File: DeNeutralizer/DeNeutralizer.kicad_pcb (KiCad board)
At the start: 2 copper layers, 27.9 x 72 mm, 20 parts, among them J1 Screw_Terminal_01x03, J2 Screw_Terminal_01x03, J3 Screw_Terminal_01x03, J4 Screw_Terminal_01x03, J5 Screw_Terminal_01x02, J6 Screw_Terminal_01x05, J7 Screw_Terminal_01x02, U1 PC817

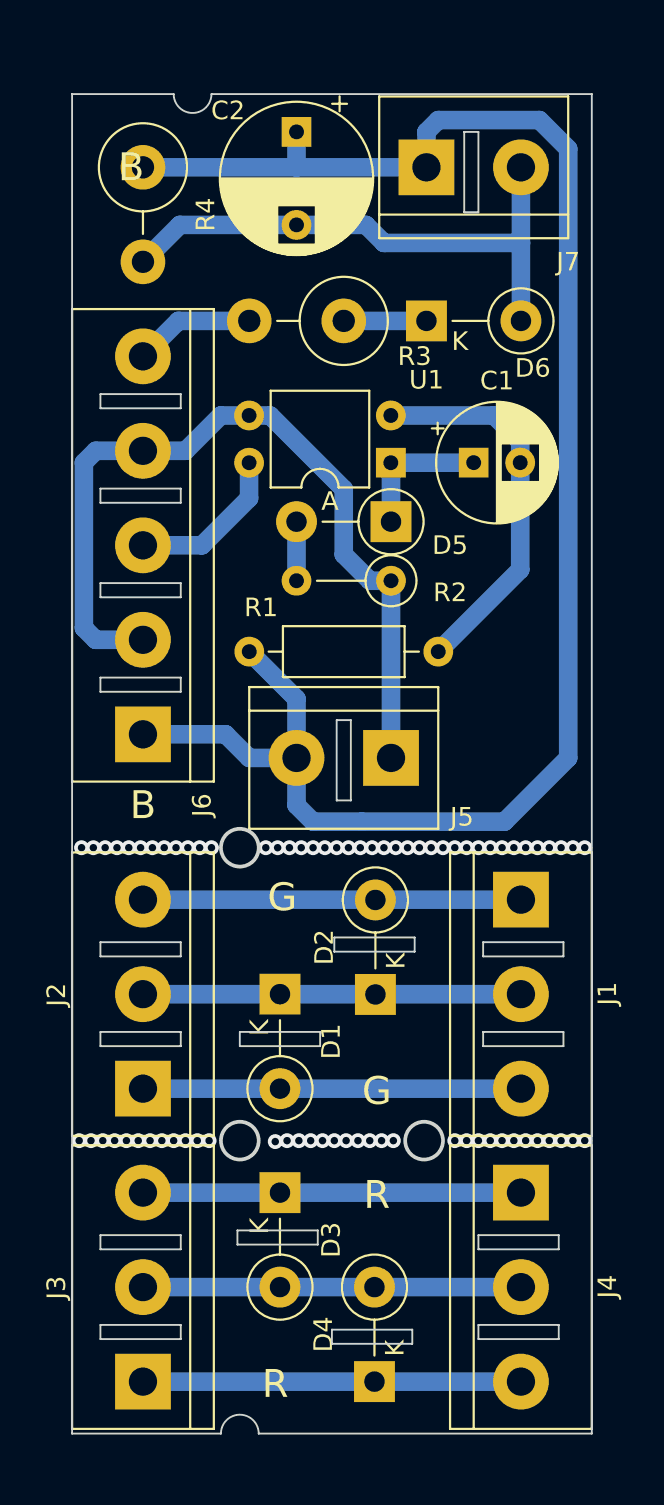
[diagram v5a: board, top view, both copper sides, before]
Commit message: Add spark gaps
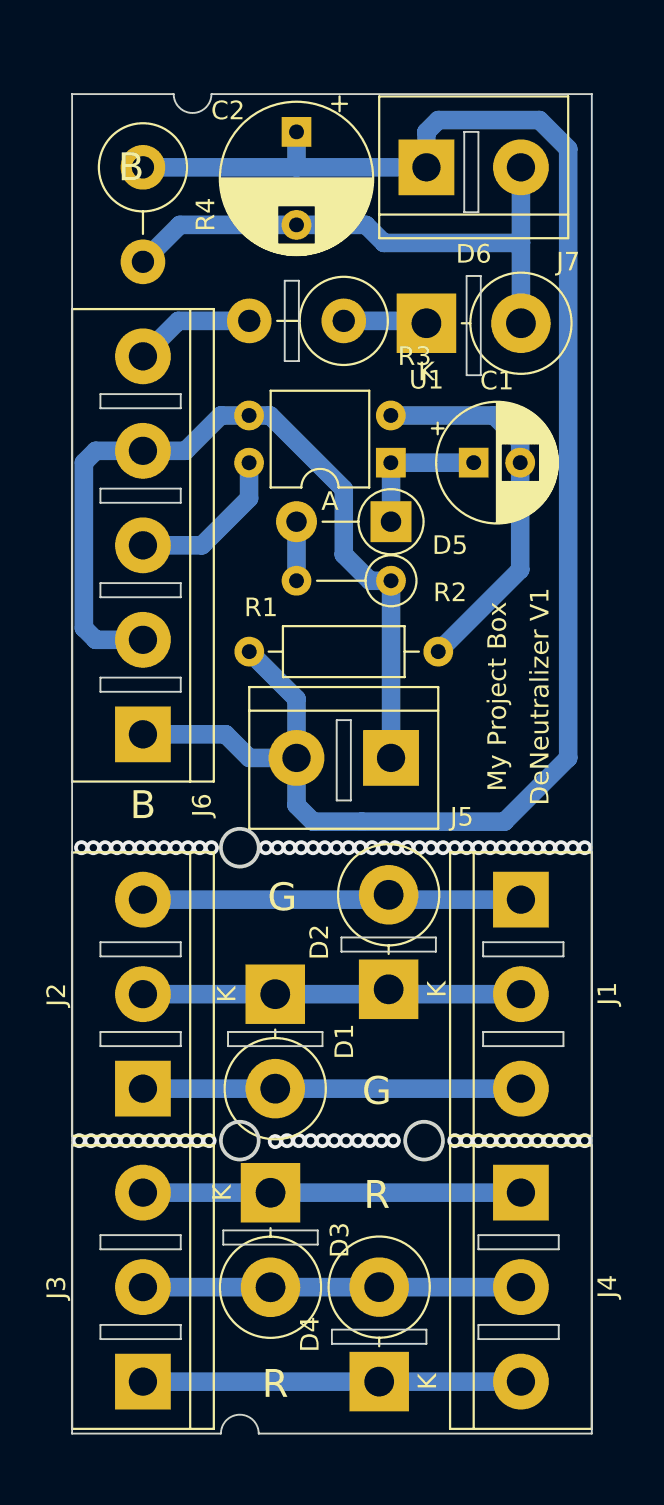
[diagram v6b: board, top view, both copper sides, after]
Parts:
- D1, D2, D3, D4, D6: value 1N4007 -> 1N5408; footprint Diode_THT:D_DO-41_SOD81_P5.08mm_Vertical_KathodeUp -> Diode_THT:D_DO-201AD_P5.08mm_Vertical_KathodeUp
- moved D2 0.76 mm to (133.9, 116.6)
- moved D3 0.51 mm to (127.5, 127.5)
- moved D1 0.25 mm to (127.8, 116.8)
- moved D4 0.25 mm to (133.3, 137.7)
- moved D6 0.13 mm to (135.9, 80.8)
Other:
- outline, holes or cut-outs redrawn
- board text added: "DeNeutralizer V1"
- board text added: "My Project Box"

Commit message: Add jumper and for switcihing between modes and crt for external ripple capacitor
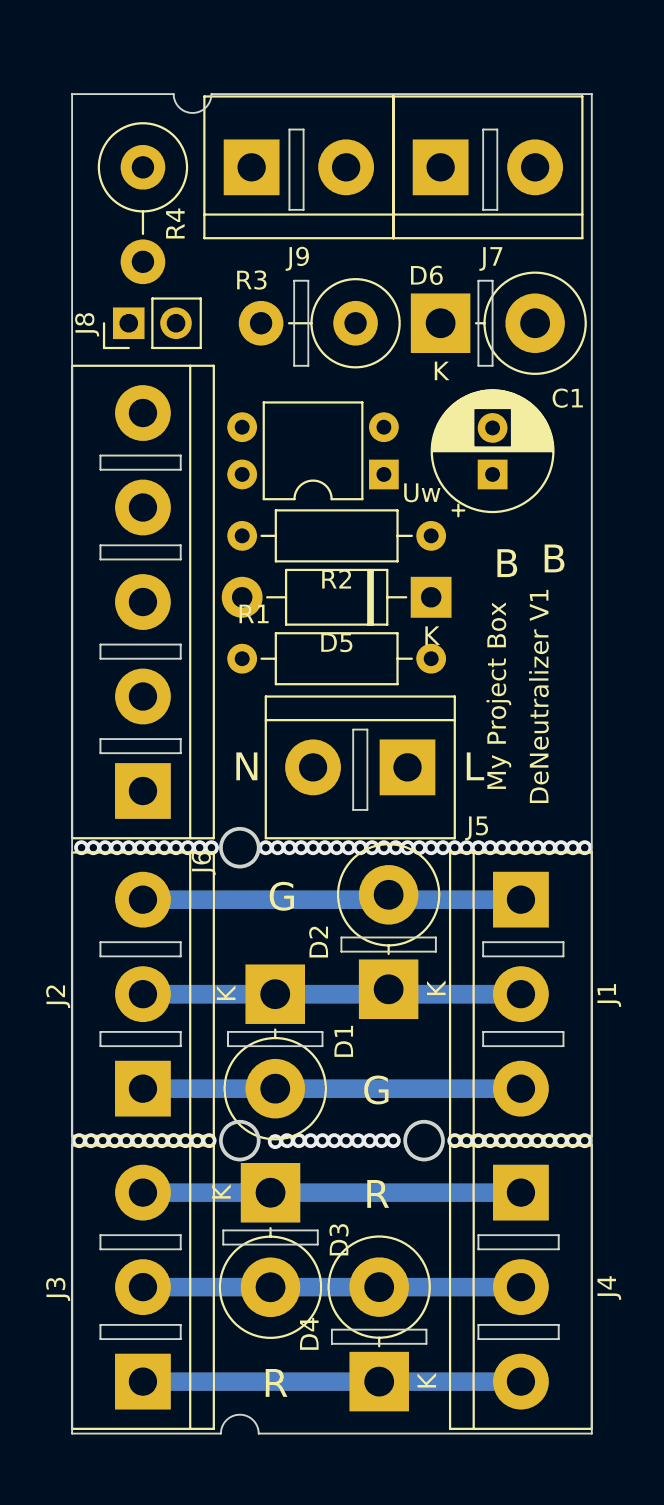
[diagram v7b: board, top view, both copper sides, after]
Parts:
- removed C2: C_Polarized, Capacitor_THT:CP_Radial_D8.0mm_P5.00mm
- added J8: Conn_01x02_Male, Connector_PinHeader_2.54mm:PinHeader_1x02_P2.54mm_Vertical, F.Cu at (119.9, 80.8)
- added J9: Ripple-Cap, TerminalBlock:TerminalBlock_bornier-2_P5.08mm, F.Cu at (126.5, 72.4)
- D5: footprint Diode_THT:D_DO-41_SOD81_P5.08mm_Vertical_AnodeUp -> Diode_THT:D_DO-41_SOD81_P10.16mm_Horizontal
- R2: footprint Resistor_THT:R_Axial_DIN0207_L6.3mm_D2.5mm_P5.08mm_Vertical -> Resistor_THT:R_Axial_DIN0207_L6.3mm_D2.5mm_P10.16mm_Horizontal
- moved D5 4.60 mm to (136.1, 95.5)
- moved R2 3.24 mm to (136.1, 92.2)
- moved J6 3.05 mm to (120.7, 105.9)
- moved C1 1.20 mm to (139.4, 88.9), turned to 90 degrees
- moved J5 1.02 mm to (134.9, 104.6)
- moved D6 0.76 mm to (136.7, 80.8)
- moved J7 0.76 mm to (136.7, 72.4)
- moved Uw 0.73 mm to (133.6, 88.9)
- moved R3 0.65 mm to (132.1, 80.8)
- moved R1 0.54 mm to (126.0, 98.8)
- renumbered U1 to Uw
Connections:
- D5 pad 1: Net-(C1-Pad1) -> Net-(R2-Pad1)
- D5 pad 2: Net-(D5-Pad2) -> Net-(J5-Pad1)
- J6 pad 4: Net-(J5-Pad1) -> Net-(J6-Pad4)
- R2 pad 1: Net-(J5-Pad1) -> Net-(R2-Pad1)
- R2 pad 2: Net-(D5-Pad2) -> Net-(C1-Pad1)
- Uw pad 3: Net-(J5-Pad1) -> Net-(J6-Pad4)
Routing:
- net Net-(J5-Pad2): track 94.8 -> 0.00 mm
- net Net-(J5-Pad1): track 45.2 -> 0.00 mm
- net Net-(D6-Pad2): track 29.9 -> 0.00 mm
- net Net-(C1-Pad2): track 20.7 -> 0.00 mm
- net Net-(J6-Pad3): track 8.67 -> 0.00 mm
- net Net-(C1-Pad1): track 7.63 -> 0.00 mm
- net Net-(J6-Pad5): track 6.50 -> 0.00 mm
- net Net-(D6-Pad1): track 4.44 -> 0.00 mm
- net Net-(D5-Pad2): track 3.17 -> 0.00 mm
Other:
- outline, holes or cut-outs redrawn
- board text added: "L"
- board text added: "N"

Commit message: Add 5W resistor insted 0.6W for serial protection
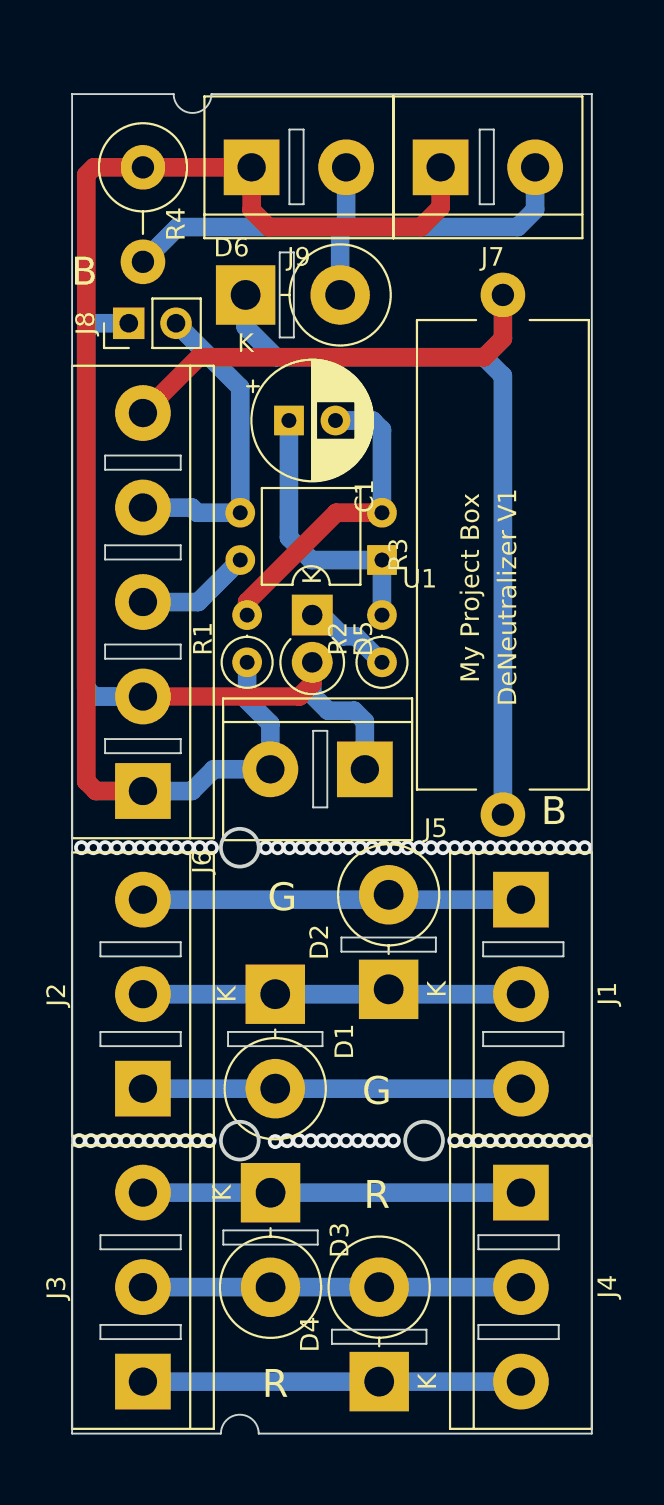
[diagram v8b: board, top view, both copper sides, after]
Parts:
- D5: footprint Diode_THT:D_DO-41_SOD81_P10.16mm_Horizontal -> Diode_THT:D_DO-41_SOD81_P2.54mm_Vertical_KathodeUp
- R1, R2: footprint Resistor_THT:R_Axial_DIN0207_L6.3mm_D2.5mm_P10.16mm_Horizontal -> Resistor_THT:R_Axial_DIN0207_L6.3mm_D2.5mm_P2.54mm_Vertical
- R3: value 10/0.6W -> 10/5W; footprint Resistor_THT:R_Axial_DIN0414_L11.9mm_D4.5mm_P5.08mm_Vertical -> Resistor_THT:R_Axial_Power_L25.0mm_W9.0mm_P27.94mm
- moved R3 27.6 mm to (140.0, 107.2), turned to 90 degrees
- moved C1 11.3 mm to (128.5, 86.0), turned to 0 degrees
- moved D6 10.6 mm to (126.2, 79.2)
- moved R2 7.29 mm to (133.5, 99.0), turned to 90 degrees
- moved D5 6.47 mm to (129.8, 96.5), turned to -90 degrees
- moved U1 4.60 mm to (133.5, 93.5)
- moved J5 2.30 mm to (132.6, 104.8)
- moved R1 0.33 mm to (126.2, 99.0), turned to 90 degrees
- renumbered Uw to U1
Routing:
- net Net-(J5-Pad2): track 0.00 -> 74.0 mm
- net Net-(D5-Pad2): track 0.00 -> 43.2 mm
- net Net-(D6-Pad1): track 0.00 -> 40.2 mm
- net Net-(D6-Pad2): track 0.00 -> 31.5 mm
- net Net-(J6-Pad5): track 0.00 -> 23.4 mm
- net Net-(C1-Pad2): track 0.00 -> 17.1 mm
- net Net-(J6-Pad4): track 0.00 -> 17.0 mm
- net Net-(C1-Pad1): track 0.00 -> 14.8 mm
- net Net-(J6-Pad3): track 0.00 -> 6.17 mm
- net Net-(D5-Pad1): track 0.00 -> 4.80 mm
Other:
- outline, holes or cut-outs redrawn
